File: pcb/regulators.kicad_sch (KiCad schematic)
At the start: 29 parts, among them U17 TPS2116DRL, U18 TPS56637RPAR, U19 ME6211C33M5

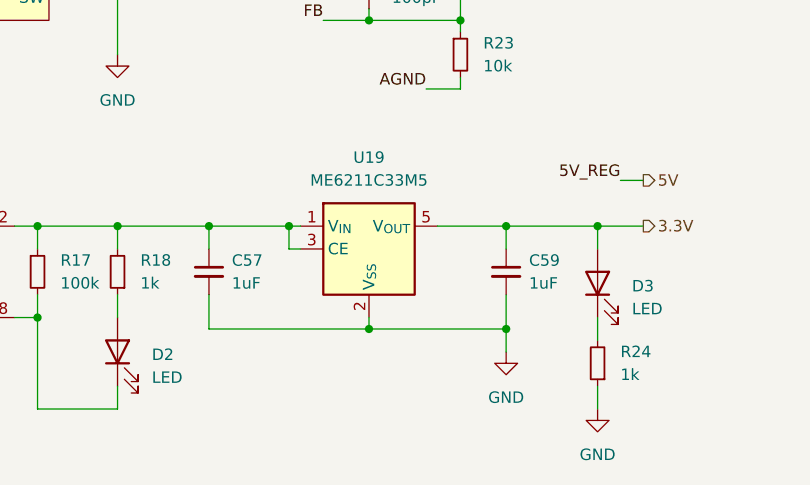
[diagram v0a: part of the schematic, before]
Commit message: fixes #3: increased input/output capacitor values for ME6211C33M5
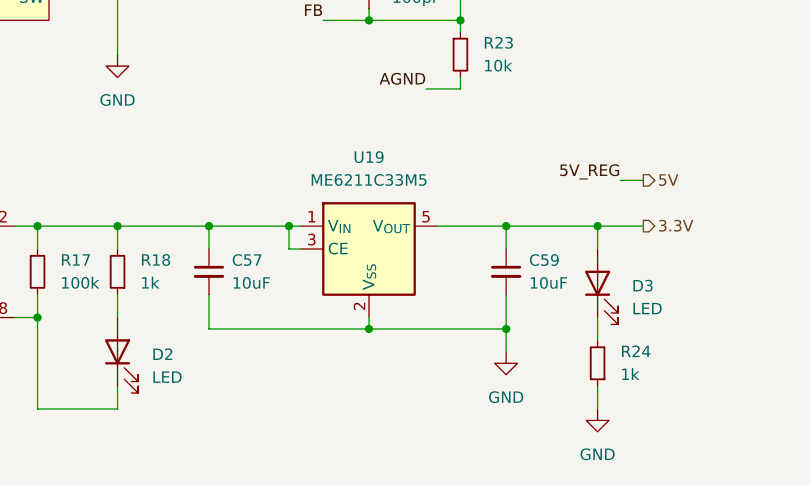
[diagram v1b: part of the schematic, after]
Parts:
- C57, C59: value 1uF -> 10uF
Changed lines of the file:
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@@
 			)
 		)
-		(property "Value" "1uF"
+		(property "Value" "10uF"
 			(at 110.49 81.2863 0)
 			(effects
@@
 			)
 		)
-		(property "Value" "1uF"
+		(property "Value" "10uF"
 			(at 143.51 81.2863 0)
 			(effects

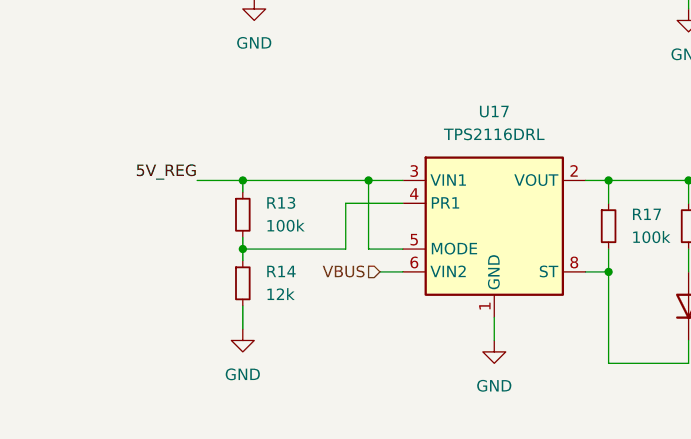
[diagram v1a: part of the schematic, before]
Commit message: fixes #2: changed resistor divider values
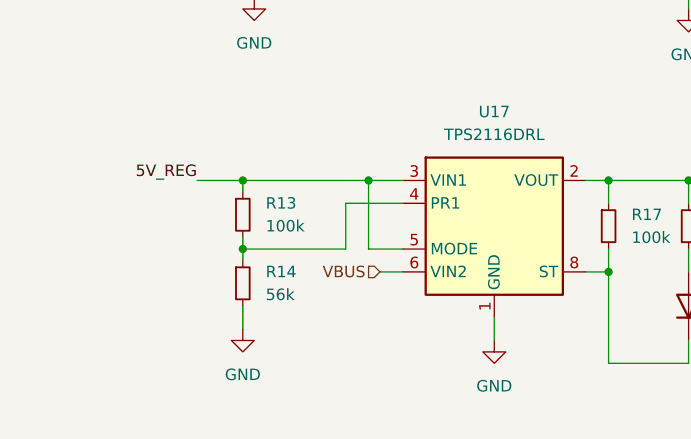
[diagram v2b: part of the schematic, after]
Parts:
- R14: value 12k -> 56k
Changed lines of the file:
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@@
 		(fields_autoplaced yes)
 		(property "Reference" "R14"
-			(at 50.8 85.09 0)
+			(at 50.8 85.0899 0)
 			(effects
 				(font
@@
 			)
 		)
-		(property "Value" "12k"
-			(at 50.8 87.63 0)
+		(property "Value" "56k"
+			(at 50.8 87.6299 0)
 			(effects
 				(font

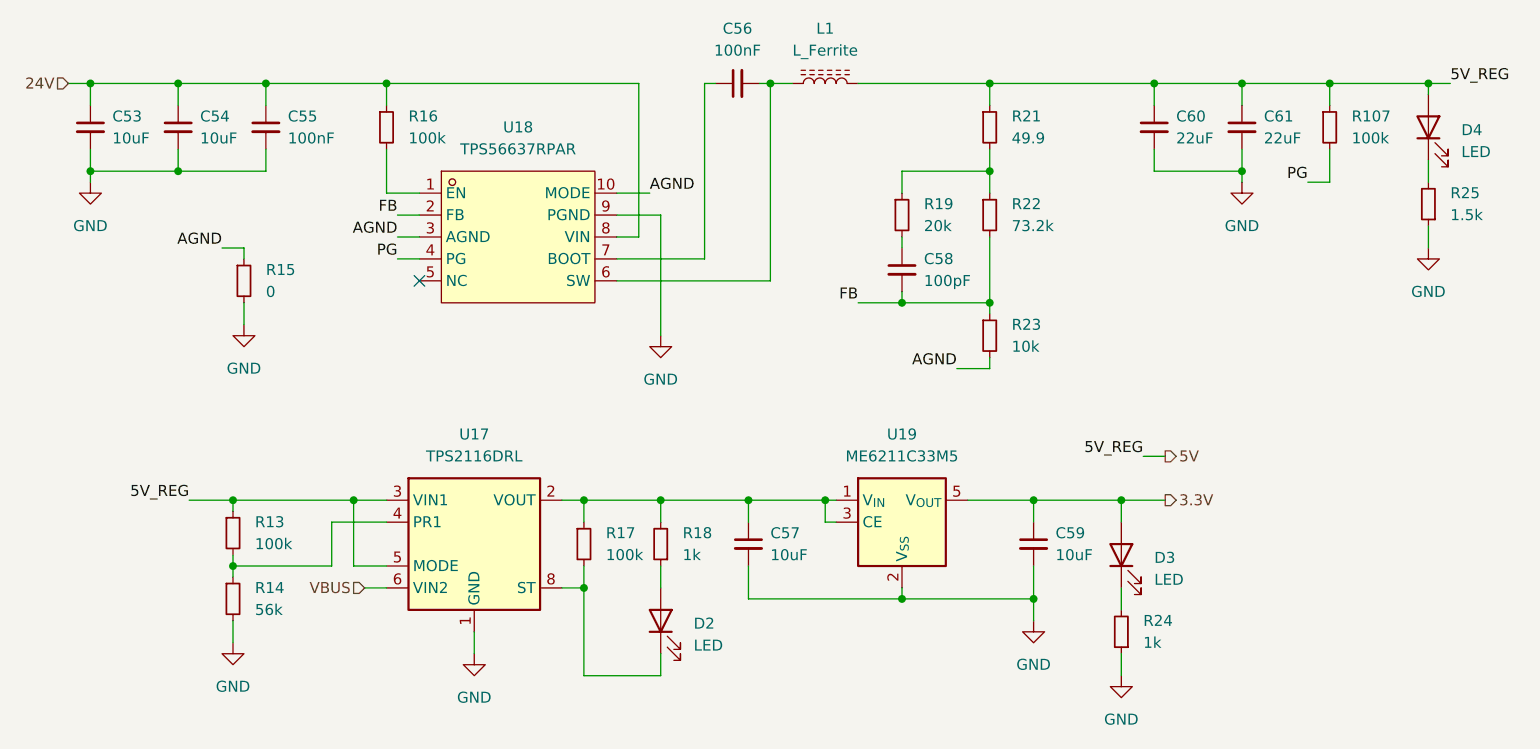
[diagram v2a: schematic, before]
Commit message: fixes #8: changed led series resistor values
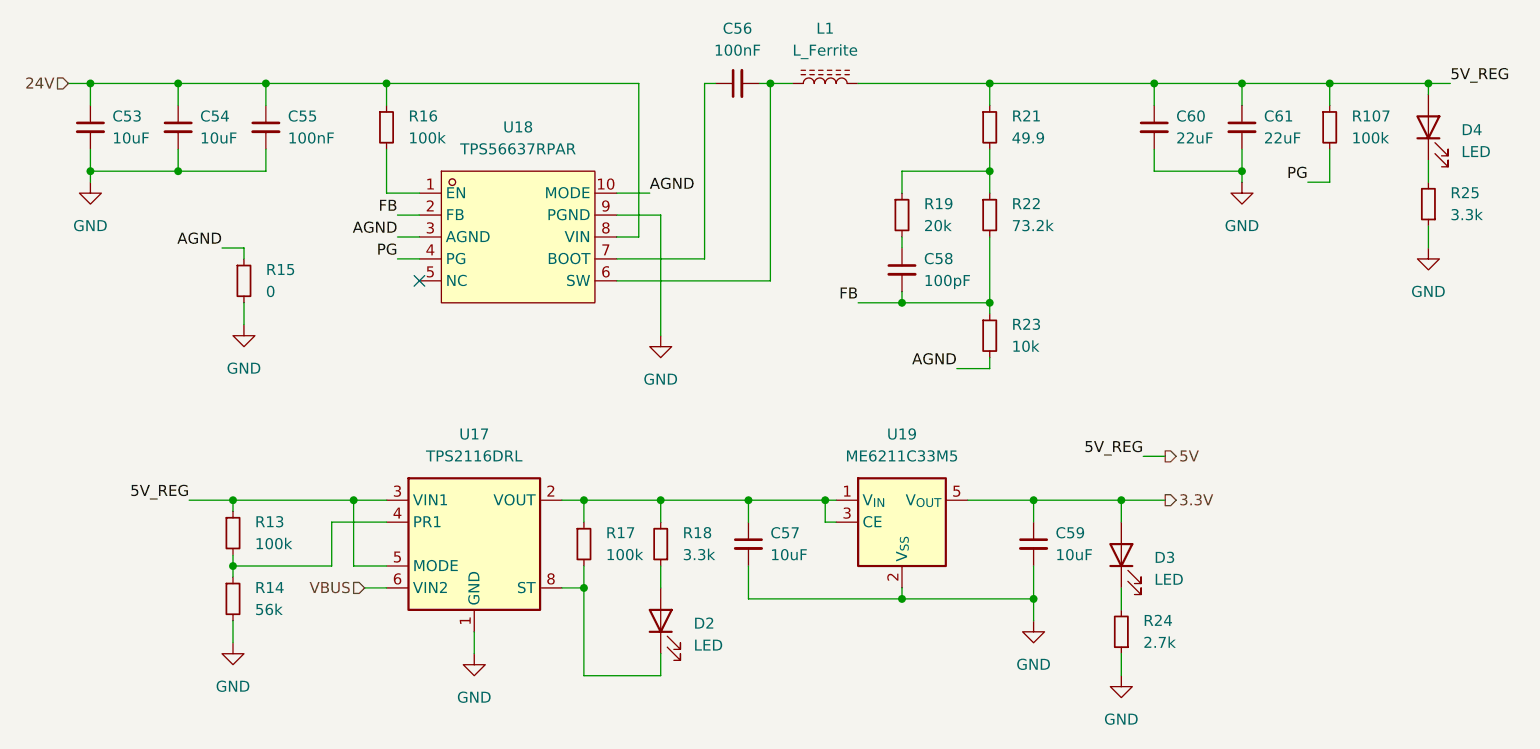
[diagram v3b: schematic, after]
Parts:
- R18: value 1k -> 3.3k
- R24: value 1k -> 2.7k
- R25: value 1.5k -> 3.3k
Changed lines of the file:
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@@
 		(fields_autoplaced yes)
 		(property "Reference" "R24"
-			(at 153.67 88.9 0)
+			(at 153.67 88.8999 0)
 			(effects
 				(font
@@
 			)
 		)
-		(property "Value" "1k"
-			(at 153.67 91.44 0)
+		(property "Value" "2.7k"
+			(at 153.67 91.4399 0)
 			(effects
 				(font
@@
 		(fields_autoplaced yes)
 		(property "Reference" "R18"
-			(at 100.33 78.74 0)
+			(at 100.33 78.7399 0)
 			(effects
 				(font
@@
 			)
 		)
-		(property "Value" "1k"
-			(at 100.33 81.28 0)
+		(property "Value" "3.3k"
+			(at 100.33 81.2799 0)
 			(effects
 				(font
@@
 		(fields_autoplaced yes)
 		(property "Reference" "R25"
-			(at 189.23 39.37 0)
+			(at 189.23 39.3699 0)
 			(effects
 				(font
@@
 			)
 		)
-		(property "Value" "1.5k"
-			(at 189.23 41.91 0)
-			(effects
-				(font
+		(property "Value" "3.3k"
+			(at 189.23 41.9099 0)
+			(effects
+				(font

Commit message: specified some values and colors added lcsc part ids for all components
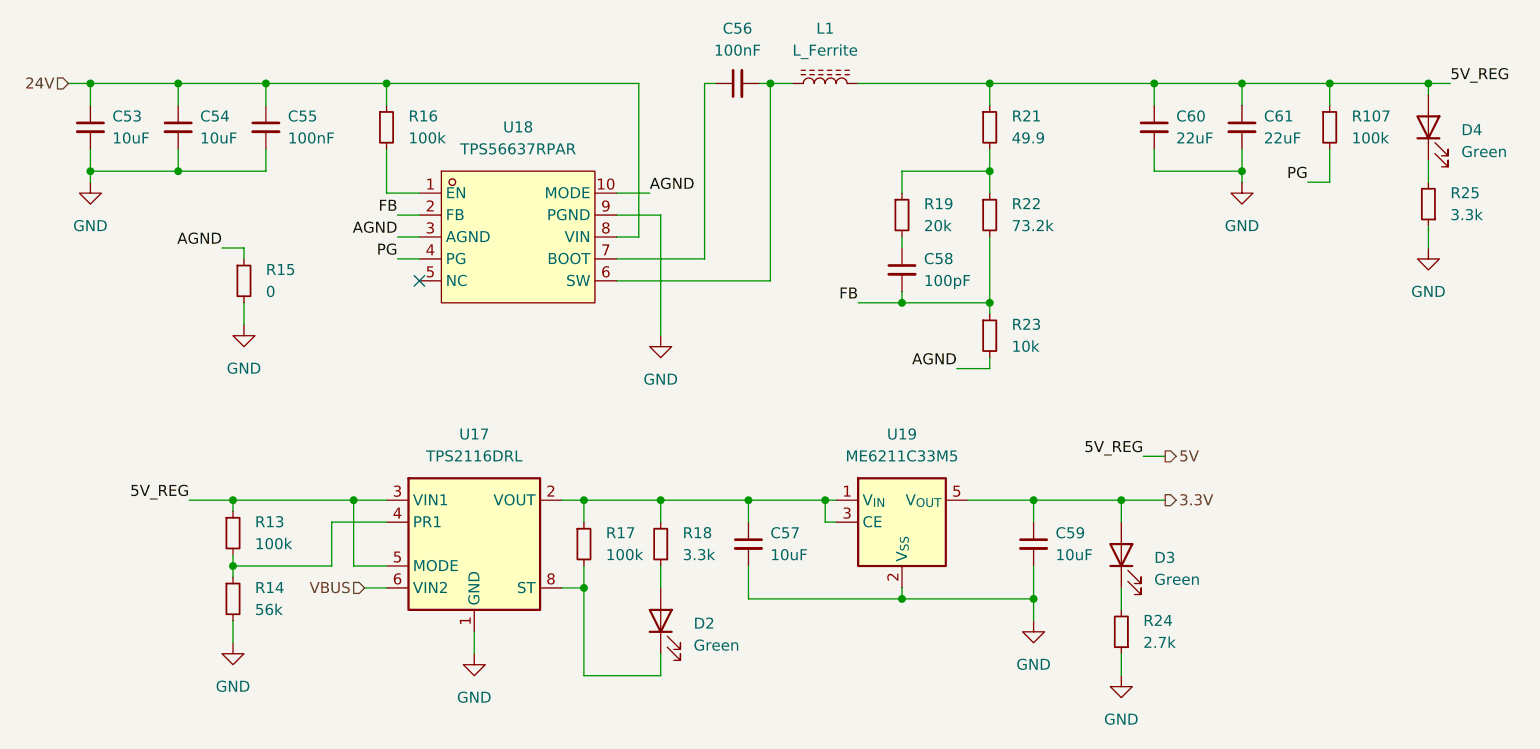
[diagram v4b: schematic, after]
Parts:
- C53, C54: LCSC (none) -> C13585
- C55, C56: LCSC (none) -> C14663
- C57, C59: LCSC (none) -> C19702
- C58: LCSC (none) -> C14665
- C60, C61: LCSC (none) -> C602037
- D2, D3, D4: value LED -> Green; LCSC (none) -> C2994781
- L1: LCSC (none) -> C7187309
- R107, R13, R16, R17: LCSC (none) -> C14675
- R14: LCSC (none) -> C23206
- R15: LCSC (none) -> C95177
- R18, R25: LCSC (none) -> C22978
- R19: LCSC (none) -> C2907011
- R21: LCSC (none) -> C114625
- R22: LCSC (none) -> C14890
- R23: LCSC (none) -> C98220
- R24: LCSC (none) -> C13167
- U17: LCSC (none) -> C3235557
- U18: LCSC (none) -> C841386
- U19: LCSC (none) -> C82942
